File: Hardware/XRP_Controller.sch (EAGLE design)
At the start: 124 parts, among them J1 POWER_JACKPOWER_JACK_SLOT, J12 Vertical Qwiic Connector, J13 Vertical Qwiic Connector, J14 Vertical Qwiic Connector, J3 JST_6_PIN_VERTICAL, J4 JST_6_PIN_VERTICAL, J5 JST_6_PIN_VERTICAL, J6 JST_6_PIN_VERTICAL, J9 Vertical Qwiic Connector, Q3 20V/4.2A/52mΩ/1.4W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

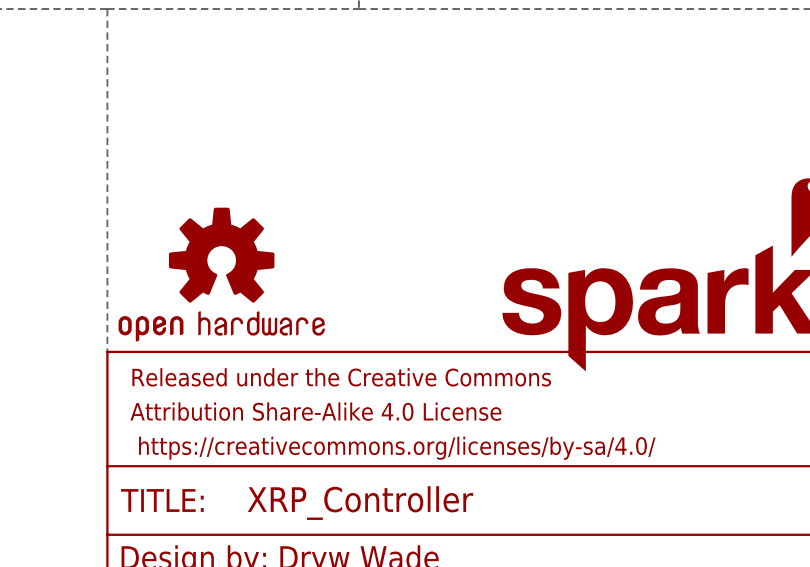
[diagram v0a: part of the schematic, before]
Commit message: Add inverted Qwiic logo as library part
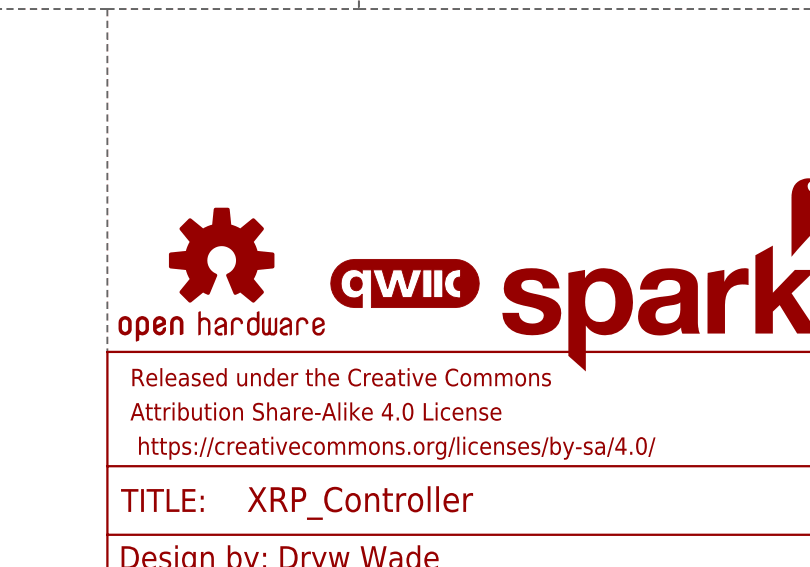
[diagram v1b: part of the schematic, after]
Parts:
- added U$98: QWIIC_LOGO, XRP_COMPONENTS:QWIIC_LOGO
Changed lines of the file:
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@@
 <part name="GND44" library="SparkFun-PowerSymbols" deviceset="GND" device=""/>
 <part name="SUPPLY40" library="SparkFun-PowerSymbols" deviceset="5V" device=""/>
+<part name="U$98" library="XRP_COMPONENTS" deviceset="QWIIC_LOGO" device=""/>
 </parts>
 <sheets>
@@
 <attribute name="VALUE" x="27.94" y="223.774" size="1.778" layer="96" font="vector" align="bottom-center"/>
 </instance>
+<instance part="U$98" gate="G$1" x="363.22" y="43.18" smashed="yes"/>
 </instances>
 <busses>

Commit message: v09 tweaks
Ordering a few boards early before logos are finalized
Removed URLs for now
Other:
- note added: "v09"
- note removed: "v10"
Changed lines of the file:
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@@
 <plain>
 <text x="358.14" y="12.7" size="2.54" layer="94" font="vector" align="center">Dryw Wade</text>
-<text x="426.72" y="7.62" size="2.54" layer="94" font="vector" align="center">v10</text>
+<text x="426.72" y="7.62" size="2.54" layer="94" font="vector" align="center">v09</text>
 <text x="396.24" y="274.32" size="2.54" layer="94" font="vector" align="center">Motor Connectors</text>
 <text x="393.7" y="137.16" size="2.54" layer="94" font="vector" align="center">Servo Connectors</text>

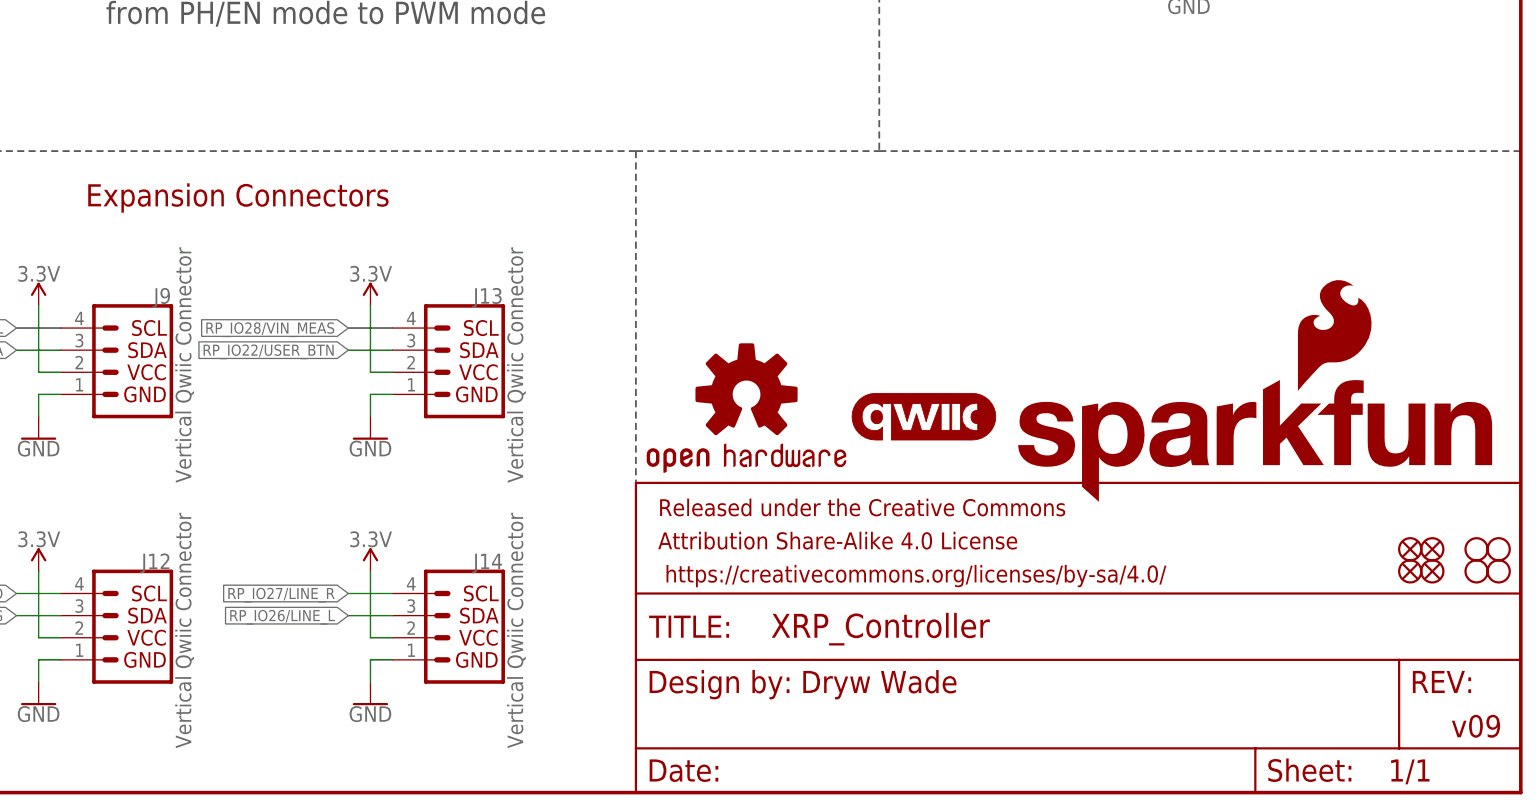
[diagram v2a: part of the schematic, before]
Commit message: v10 updates
Bump version number to v10
Remove OpenSTEM logo
Add XRP URL to top and bottom silk
Nudge expansion connectors in schematic to not have overlapping labels
Nudge Qwiic logo to get thicker silk along bottom edge
Approve DRC overlap errors
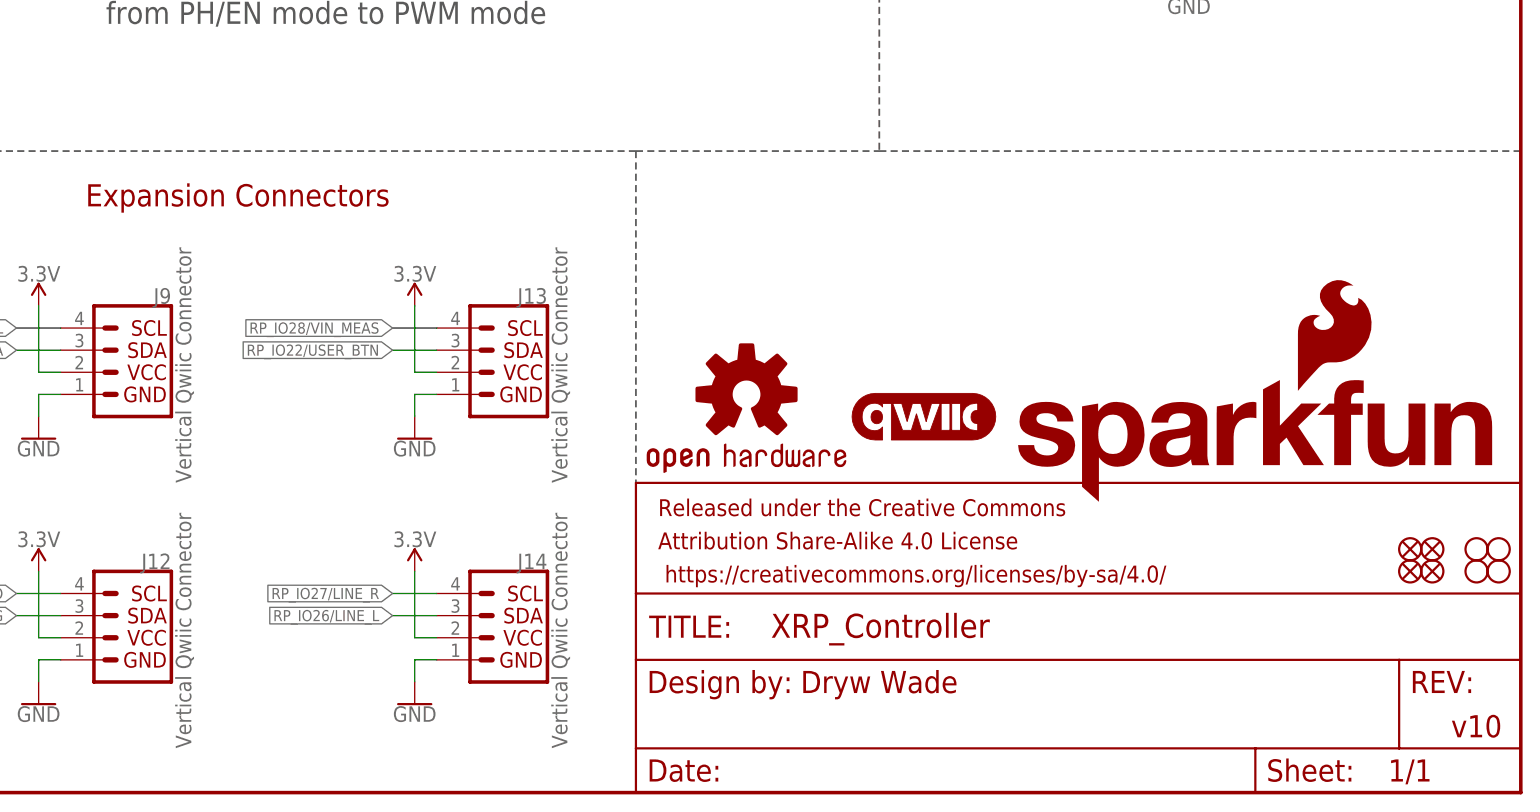
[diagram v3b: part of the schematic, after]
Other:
- note added: "v10"
- note removed: "v09"
- moved on the sheet: J13, J14
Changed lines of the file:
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@@
 <plain>
 <text x="358.14" y="12.7" size="2.54" layer="94" font="vector" align="center">Dryw Wade</text>
-<text x="426.72" y="7.62" size="2.54" layer="94" font="vector" align="center">v09</text>
+<text x="426.72" y="7.62" size="2.54" layer="94" font="vector" align="center">v10</text>
 <text x="396.24" y="274.32" size="2.54" layer="94" font="vector" align="center">Motor Connectors</text>
 <text x="393.7" y="137.16" size="2.54" layer="94" font="vector" align="center">Servo Connectors</text>
@@
 <attribute name="NAME" x="276.86" y="25.654" size="1.778" layer="95" font="vector" rot="MR0"/>
 </instance>
-<instance part="J13" gate="G$1" x="309.88" y="48.26" smashed="yes" rot="MR0">
-<attribute name="VALUE" x="317.246" y="35.56" size="1.778" layer="96" font="vector" rot="MR90" align="top-left"/>
-<attribute name="NAME" x="314.96" y="56.134" size="1.778" layer="95" font="vector" rot="MR0"/>
-</instance>
-<instance part="J14" gate="G$1" x="309.88" y="17.78" smashed="yes" rot="MR0">
-<attribute name="VALUE" x="317.246" y="5.08" size="1.778" layer="96" font="vector" rot="MR90" align="top-left"/>
-<attribute name="NAME" x="314.96" y="25.654" size="1.778" layer="95" font="vector" rot="MR0"/>
+<instance part="J13" gate="G$1" x="314.96" y="48.26" smashed="yes" rot="MR0">
+<attribute name="VALUE" x="322.326" y="35.56" size="1.778" layer="96" font="vector" rot="MR90" align="top-left"/>
+<attribute name="NAME" x="320.04" y="56.134" size="1.778" layer="95" font="vector" rot="MR0"/>
+</instance>
+<instance part="J14" gate="G$1" x="314.96" y="17.78" smashed="yes" rot="MR0">
+<attribute name="VALUE" x="322.326" y="5.08" size="1.778" layer="96" font="vector" rot="MR90" align="top-left"/>
+<attribute name="NAME" x="320.04" y="25.654" size="1.778" layer="95" font="vector" rot="MR0"/>
 </instance>
 <instance part="GND1" gate="1" x="22.86" y="5.08" smashed="yes">
@@
 <attribute name="VALUE" x="261.62" y="28.194" size="1.778" layer="96" font="vector" align="bottom-center"/>
 </instance>
-<instance part="GND7" gate="1" x="299.72" y="40.64" smashed="yes">
-<attribute name="VALUE" x="299.72" y="40.386" size="1.778" layer="96" font="vector" align="top-center"/>
-</instance>
-<instance part="SUPPLY9" gate="G$1" x="299.72" y="55.88" smashed="yes">
-<attribute name="VALUE" x="299.72" y="58.674" size="1.778" layer="96" font="vector" align="bottom-center"/>
-</instance>
-<instance part="GND8" gate="1" x="299.72" y="10.16" smashed="yes">
-<attribute name="VALUE" x="299.72" y="9.906" size="1.778" layer="96" font="vector" align="top-center"/>
-</instance>
-<instance part="SUPPLY10" gate="G$1" x="299.72" y="25.4" smashed="yes">
-<attribute name="VALUE" x="299.72" y="28.194" size="1.778" layer="96" font="vector" align="bottom-center"/>
+<instance part="GND7" gate="1" x="304.8" y="40.64" smashed="yes">
+<attribute name="VALUE" x="304.8" y="40.386" size="1.778" layer="96" font="vector" align="top-center"/>
+</instance>
+<instance part="SUPPLY9" gate="G$1" x="304.8" y="55.88" smashed="yes">
+<attribute name="VALUE" x="304.8" y="58.674" size="1.778" layer="96" font="vector" align="bottom-center"/>
+</instance>
+<instance part="GND8" gate="1" x="304.8" y="10.16" smashed="yes">
+<attribute name="VALUE" x="304.8" y="9.906" size="1.778" layer="96" font="vector" align="top-center"/>
+</instance>
+<instance part="SUPPLY10" gate="G$1" x="304.8" y="25.4" smashed="yes">
+<attribute name="VALUE" x="304.8" y="28.194" size="1.778" layer="96" font="vector" align="bottom-center"/>
 </instance>
 <instance part="SUPPLY11" gate="G$1" x="10.16" y="91.44" smashed="yes">
@@
 </segment>
 <segment>
-<wire x1="299.72" y1="45.72" x2="299.72" y2="43.18" width="0.1524" layer="91"/>
-<wire x1="299.72" y1="45.72" x2="302.26" y2="45.72" width="0.1524" layer="91"/>
+<wire x1="304.8" y1="45.72" x2="304.8" y2="43.18" width="0.1524" layer="91"/>
+<wire x1="304.8" y1="45.72" x2="307.34" y2="45.72" width="0.1524" layer="91"/>
 <pinref part="J13" gate="G$1" pin="1"/>
 <pinref part="GND7" gate="1" pin="GND"/>
 </segment>
 <segment>
-<wire x1="299.72" y1="15.24" x2="299.72" y2="12.7" width="0.1524" layer="91"/>
-<wire x1="299.72" y1="15.24" x2="302.26" y2="15.24" width="0.1524" layer="91"/>
+<wire x1="304.8" y1="15.24" x2="304.8" y2="12.7" width="0.1524" layer="91"/>
+<wire x1="304.8" y1="15.24" x2="307.34" y2="15.24" width="0.1524" layer="91"/>
 <pinref part="J14" gate="G$1" pin="1"/>
 <pinref part="GND8" gate="1" pin="GND"/>
@@
 </segment>
 <segment>
-<wire x1="299.72" y1="48.26" x2="299.72" y2="55.88" width="0.1524" layer="91"/>
-<wire x1="302.26" y1="48.26" x2="299.72" y2="48.26" width="0.1524" layer="91"/>
+<wire x1="304.8" y1="48.26" x2="304.8" y2="55.88" width="0.1524" layer="91"/>
+<wire x1="307.34" y1="48.26" x2="304.8" y2="48.26" width="0.1524" layer="91"/>
 <pinref part="J13" gate="G$1" pin="2"/>
 <pinref part="SUPPLY9" gate="G$1" pin="3.3V"/>
 </segment>
 <segment>
-<wire x1="299.72" y1="17.78" x2="299.72" y2="25.4" width="0.1524" layer="91"/>
-<wire x1="302.26" y1="17.78" x2="299.72" y2="17.78" width="0.1524" layer="91"/>
+<wire x1="304.8" y1="17.78" x2="304.8" y2="25.4" width="0.1524" layer="91"/>
+<wire x1="307.34" y1="17.78" x2="304.8" y2="17.78" width="0.1524" layer="91"/>
 <pinref part="J14" gate="G$1" pin="2"/>
 <pinref part="SUPPLY10" gate="G$1" pin="3.3V"/>
@@
 </segment>
 <segment>
-<wire x1="302.26" y1="50.8" x2="297.18" y2="50.8" width="0.1524" layer="91"/>
-<label x="297.18" y="50.8" size="1.27" layer="95" font="vector" rot="R180" xref="yes"/>
+<wire x1="307.34" y1="50.8" x2="302.26" y2="50.8" width="0.1524" layer="91"/>
+<label x="302.26" y="50.8" size="1.27" layer="95" font="vector" rot="R180" xref="yes"/>
 <pinref part="J13" gate="G$1" pin="3"/>
 </segment>
@@
 </segment>
 <segment>
-<wire x1="302.26" y1="20.32" x2="297.18" y2="20.32" width="0.1524" layer="91"/>
-<label x="297.18" y="20.32" size="1.27" layer="95" font="vector" rot="R180" xref="yes"/>
+<wire x1="307.34" y1="20.32" x2="302.26" y2="20.32" width="0.1524" layer="91"/>
+<label x="302.26" y="20.32" size="1.27" layer="95" font="vector" rot="R180" xref="yes"/>
 <pinref part="J14" gate="G$1" pin="3"/>
 </segment>
@@
 </segment>
 <segment>
-<wire x1="302.26" y1="22.86" x2="297.18" y2="22.86" width="0.1524" layer="91"/>
-<label x="297.18" y="22.86" size="1.27" layer="95" font="vector" rot="R180" xref="yes"/>
+<wire x1="307.34" y1="22.86" x2="302.26" y2="22.86" width="0.1524" layer="91"/>
+<label x="302.26" y="22.86" size="1.27" layer="95" font="vector" rot="R180" xref="yes"/>
 <pinref part="J14" gate="G$1" pin="4"/>
 </segment>
@@
 </segment>
 <segment>
-<wire x1="302.26" y1="53.34" x2="297.18" y2="53.34" width="0.1524" layer="91"/>
-<label x="297.18" y="53.34" size="1.27" layer="95" font="vector" rot="R180" xref="yes"/>
+<wire x1="307.34" y1="53.34" x2="302.26" y2="53.34" width="0.1524" layer="91"/>
+<label x="302.26" y="53.34" size="1.27" layer="95" font="vector" rot="R180" xref="yes"/>
 <pinref part="J13" gate="G$1" pin="4"/>
 </segment>
